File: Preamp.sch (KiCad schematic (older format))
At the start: 138 parts, among them J1 Conn_01x03, J10 RCAJack, J11 XLR4BODYPIN, J12 XLR4BODYPIN, J13 XLR4BODYPIN, J2 Conn_01x02, J3 Conn_01x02, J4 RCAJack, J5 RCAJack, J6 Conn_01x01, J7 Conn_01x01, J8 Conn_01x01, J9 Conn_01x01, SW1 SW_SPST, U1 LM317, U2 LM337, U3 LM4562, U4 LM4562, U5 LM4562, U6 LM4562, U7 LM4562, U8 LM4562

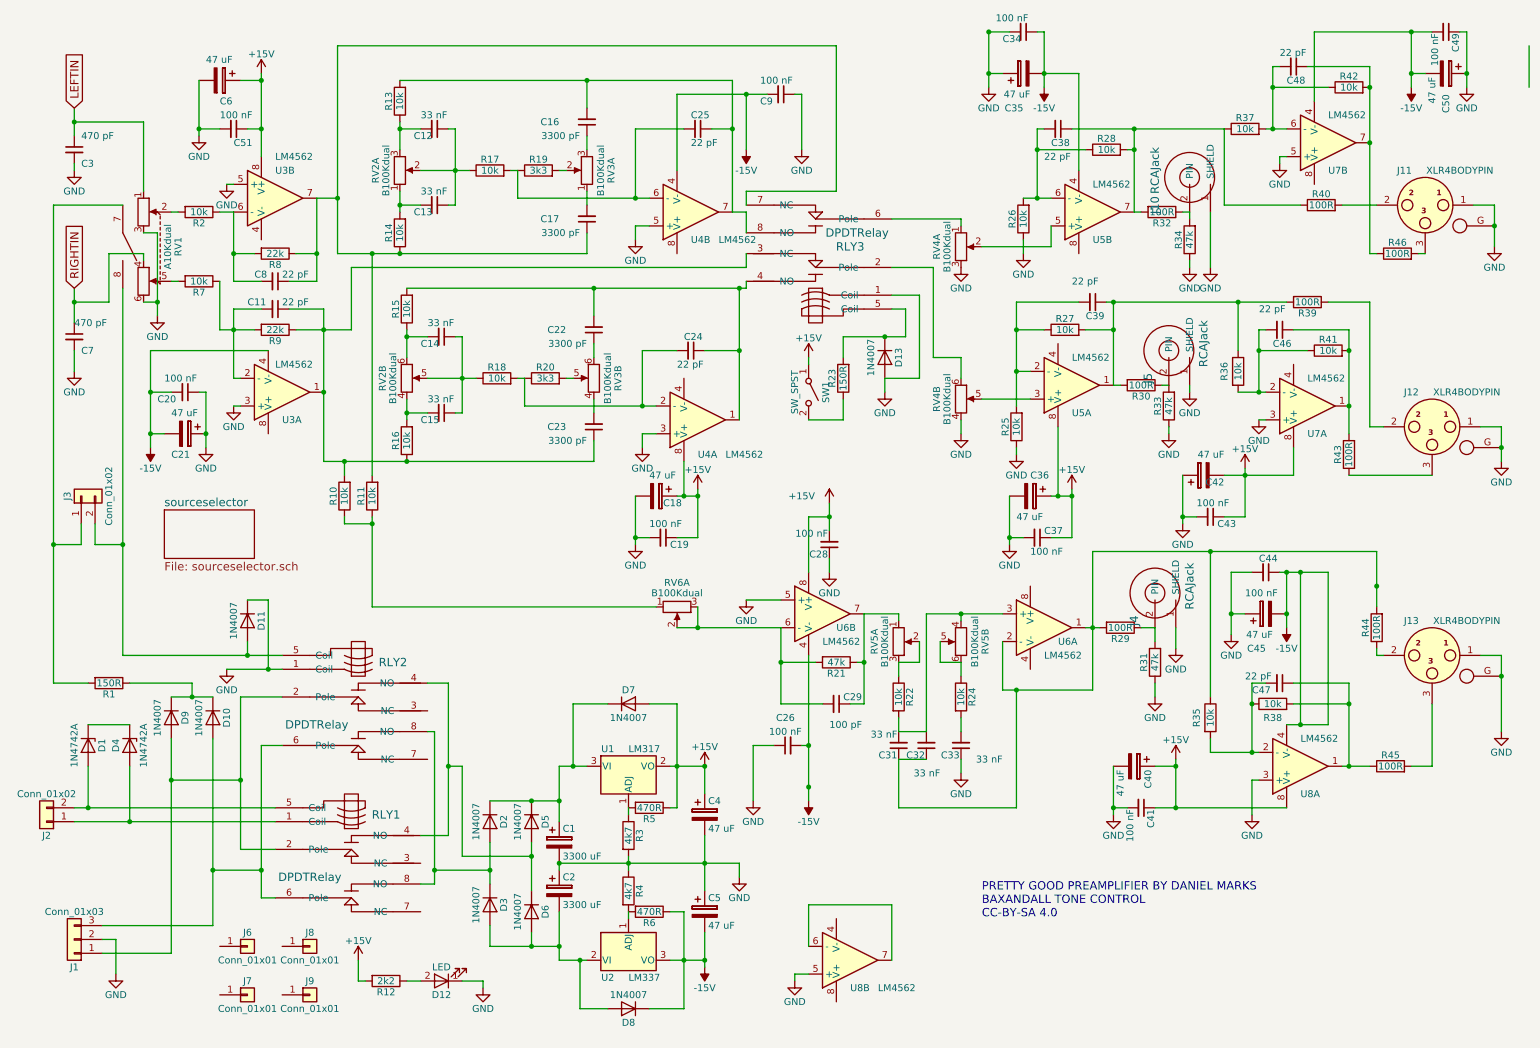
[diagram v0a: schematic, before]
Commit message: Changed balanced output to THAT1646
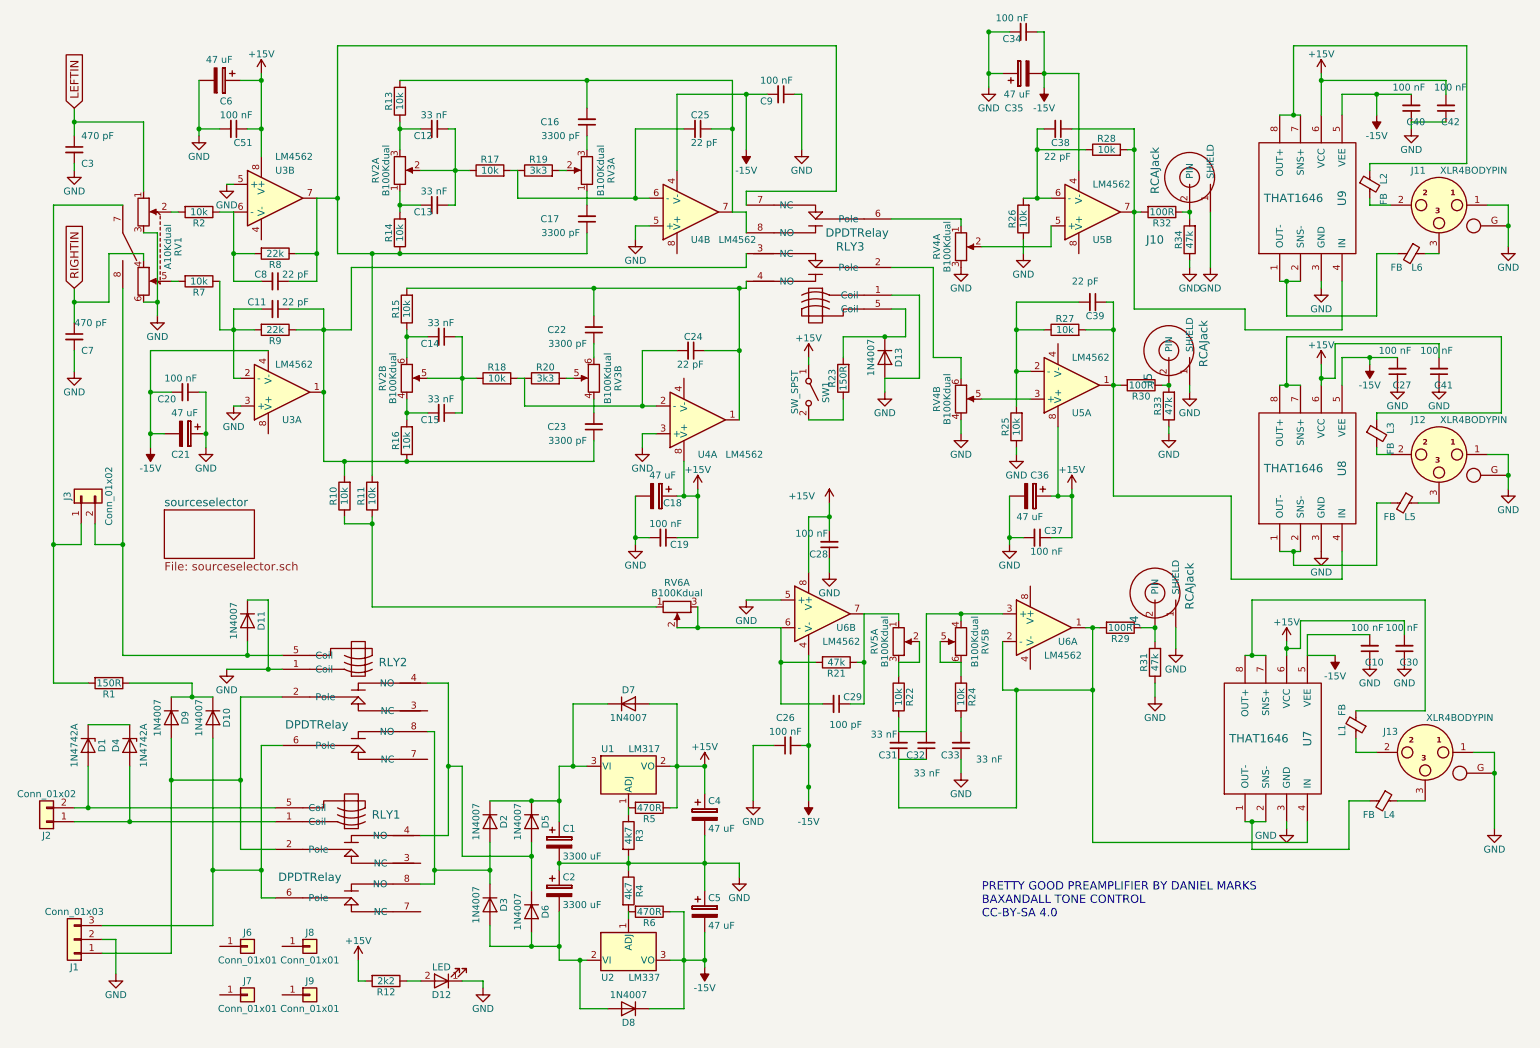
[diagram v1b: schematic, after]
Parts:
- removed C40, C42, C45, C50: 47 uF, Capacitors_THT:CP_Radial_D5.0mm_P2.50mm, symbol CP
- removed C43, C44, C49: 100 nF, Capacitors_THT:C_Disc_D5.0mm_W2.5mm_P5.00mm, symbol C_Small
- removed C46, C47, C48: 22 pF, Capacitors_THT:C_Disc_D5.0mm_W2.5mm_P5.00mm, symbol C_Small
- removed R35, R36, R37, R38, R41, R42: 10k, Resistors_THT:R_Axial_DIN0207_L6.3mm_D2.5mm_P7.62mm_Horizontal, symbol R
- removed R39, R40, R43, R44, R45, R46: 100R, Resistors_THT:R_Axial_DIN0207_L6.3mm_D2.5mm_P7.62mm_Horizontal, symbol R
- removed U7, U8: LM4562, Housings_DIP:DIP-8_W7.62mm, symbol TL072
- added C10, C27, C30, C40, C42: 100 nF, Capacitors_THT:C_Disc_D5.0mm_W2.5mm_P5.00mm, symbol C_Small
- added L1, L2, L3, L4, L5, L6: FB, Inductors_THT:L_Axial_L7.0mm_D3.3mm_P10.16mm_Horizontal_Fastron_MICC, symbol Ferrite_Bead_Small
- added U7, U8, U9: THAT1646, Housings_DIP:DIP-8_W7.62mm_Socket, symbol THAT1646
- U3, U4, U5, U6: footprint Housings_DIP:DIP-8_W7.62mm -> Housings_DIP:DIP-8_W7.62mm_Socket
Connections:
- net +15V: now also C41.2, C30.2, C42.2, U7.6 (VCC), U8.6 (VCC), U9.6 (VCC); no longer C41.1
- net -15V: now also C10.2, C27.2, C40.2, U7.5 (VEE), U8.5 (VEE), U9.5 (VEE)
- net GND: now also C41.1, C10.1, C27.1, C30.1, C40.1, C42.1, U7.3 (GND), U8.3 (GND), U9.3 (GND); no longer C41.2
- net at C31.1, C32.1, R29.2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: now also U7.4 (IN)
- net at J12.2: now also L3.2
- net at C39.1, R27.2, R30.2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: now also U8.4 (IN)
- net at J11.3: now also L6.1
- net at C38.1, R28.2, R32.2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: now also U9.4 (IN)
- net at J13.2: now also L1.1
- net at J12.3: now also L5.1
- net at J11.2: now also L2.2
- net at J13.3: now also L4.1
- new net: L6.2, U9.1 (OUT-), U9.2 (SNS-)
- new net: L2.1, U9.7 (SNS+), U9.8 (OUT+)
- new net: L5.2, U8.1 (OUT-), U8.2 (SNS-)
- new net: L3.1, U8.7 (SNS+), U8.8 (OUT+)
- new net: L4.2, U7.1 (OUT-), U7.2 (SNS-)
- new net: L1.2, U7.7 (SNS+), U7.8 (OUT+)
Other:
- moved on the sheet: J11, J12, J13

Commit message: Changed one input to be balanced
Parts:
- added C49, C52, C53: 47 uF, Capacitors_THT:CP_Radial_D5.0mm_P2.50mm, symbol CP
- added J25, J26, J27, J28: Conn_01x01, Connectors:1pin, symbol Conn_01x01
- added R34: 47k, Resistors_THT:R_Axial_DIN0207_L6.3mm_D2.5mm_P7.62mm_Horizontal, symbol R
- added R35, R36: 10k, Resistors_THT:R_Axial_DIN0207_L6.3mm_D2.5mm_P7.62mm_Horizontal, symbol R
- C50: renamed from R34; value 47k -> 47 uF; footprint Resistors_THT:R_Axial_DIN0207_L6.3mm_D2.5mm_P7.62mm_Horizontal -> Capacitors_THT:CP_Radial_D5.0mm_P2.50mm; symbol R -> CP
- R8, R9: value 22k -> 47k
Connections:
- net GND: now also R34.1; no longer C50.1
- net LEFTIN: now also C53.2; no longer C3.1, RV1.1
- net RIGHTIN: now also C52.2; no longer C7.1, RV1.4
- net at J10.2 (PIN), R32.1: now also R34.2; no longer C50.2
- new net: C50.2, C7.1, R36.1
- new net: C3.1, C49.2, R35.2
- new net: R35.1, RV1.1
- new net: R36.2, RV1.4
- new net: C49.1, C53.1
- new net: C50.1, C52.1
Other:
- moved on the sheet: C7, J6, J7, J8, J9

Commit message: JLCPCB 2021-03-26
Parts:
- RV1: footprint Preamp:Dual_Potentiometer_Switch_WirePads -> Preamp:Dual_Potentiometer_Switch_Wide_WirePads
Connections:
- no-connect marks 0 -> 12
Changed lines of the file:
@@
 F 0 "RV1" H 1400 2300 50  0000 C CNN
 F 1 "A10Kdual" H 1400 2225 50  0000 C CNN
-F 2 "Preamp:Dual_Potentiometer_Switch_WirePads" H 1650 2075 50  0001 C CNN
+F 2 "Preamp:Dual_Potentiometer_Switch_Wide_WirePads" H 1650 2075 50  0001 C CNN
 F 3 "" H 1650 2075 50  0001 C CNN
 	1    1400 2150
@@
 	4800 6950 4800 7000
 Wire Wire Line
-	4300 7300 4500 7300
-Wire Wire Line
 	4300 5900 4500 5900
 Wire Wire Line
@@
 Wire Wire Line
 	800  2450 800  2350
+Wire Wire Line
+	4300 7300 4500 7300
+NoConn ~ 2300 7100
+NoConn ~ 1850 7100
+NoConn ~ 1850 7400
+NoConn ~ 2300 7400
+NoConn ~ 2300 7700
+NoConn ~ 1850 7700
+NoConn ~ 1400 7700
+NoConn ~ 950  7700
+NoConn ~ 3300 6950
+NoConn ~ 3300 6600
+NoConn ~ 3350 5850
+NoConn ~ 3350 5500
 $EndSCHEMATC

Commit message: Pre off relay
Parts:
- removed R23: 150R, Resistors_THT:R_Axial_DIN0309_L9.0mm_D3.2mm_P12.70mm_Horizontal, symbol R
- added R37, R38, R39, R40: NC, Resistors_THT:R_Axial_DIN0207_L6.3mm_D2.5mm_P7.62mm_Horizontal, symbol R
- added R41, R42: 100R, Resistors_THT:R_Axial_DIN0411_L9.9mm_D3.6mm_P12.70mm_Horizontal, symbol R
- R10, R11: value 10k -> 47k
- R2, R7: value 10k -> 4k7
- R5, R6: value 470R -> 560R
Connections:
- net +15V: now also R41.1
- net -15V: now also C26.1, R42.2; no longer C26.2
- net GND: now also C26.2, D11.2 (A), R37.1, R38.2, R41.2, R42.1; no longer C26.1, D11.1 (K)
- net at R2.2, RV1.2: now also R37.2
- net at R7.2, RV1.5: now also R38.1
- net at J3.2 (Pin_2), RLY2.5 (Coil), RV1.8: now also D11.1 (K); no longer D11.2 (A)
- net at RLY3.6 (Pole), RV4.1 (4): now also R40.2
- net at RV4.2 (5), U5.5 (+): now also R40.1
- net at RV4.5, U5.3 (+): now also R39.1
- net at RLY3.2 (Pole), RV4.6: now also R39.2
- net at D13.1 (K), RLY3.5 (Coil): now also SW1.2 (B)
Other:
- moved on the sheet: C26

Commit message: Tried a relay version out
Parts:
- removed R41, R42: 100R, Resistors_THT:R_Axial_DIN0411_L9.9mm_D3.6mm_P12.70mm_Horizontal, symbol R
- C1, C2: value 3300 uF -> 47 uF; footprint Capacitors_THT:CP_Radial_D10.0mm_P5.00mm -> Capacitors_THT:CP_Radial_D7.5mm_P2.50mm
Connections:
- net at D9.2 (A), J1.1 (Pin_1), RLY1.2 (Pole): now also RLY2.6 (Pole); no longer RLY2.2 (Pole)
- net at D10.2 (A), J1.3 (Pin_3), RLY1.6 (Pole): now also RLY2.2 (Pole); no longer RLY2.6 (Pole)
- net at D2.2 (A), D3.1 (K), RLY1.8 (NO): now also RLY2.4 (NO); no longer RLY2.8 (NO)
- net at D5.2 (A), D6.1 (K), RLY1.4 (NO): now also RLY2.8 (NO); no longer RLY2.4 (NO)

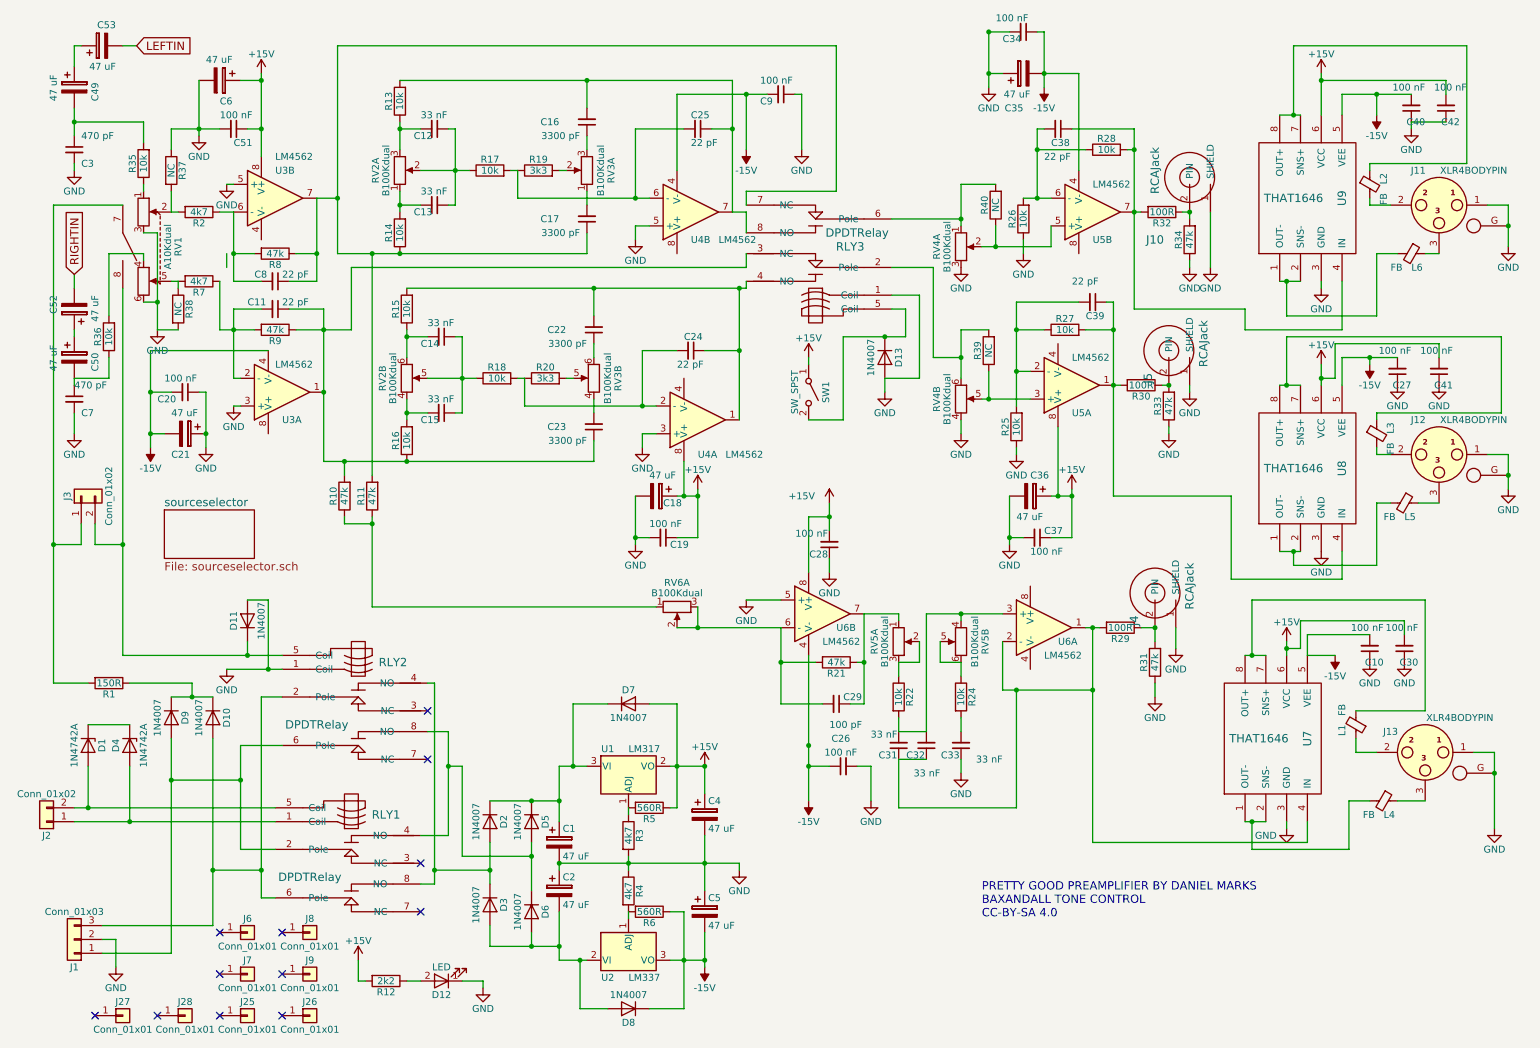
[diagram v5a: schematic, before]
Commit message: Put larger capacitors on
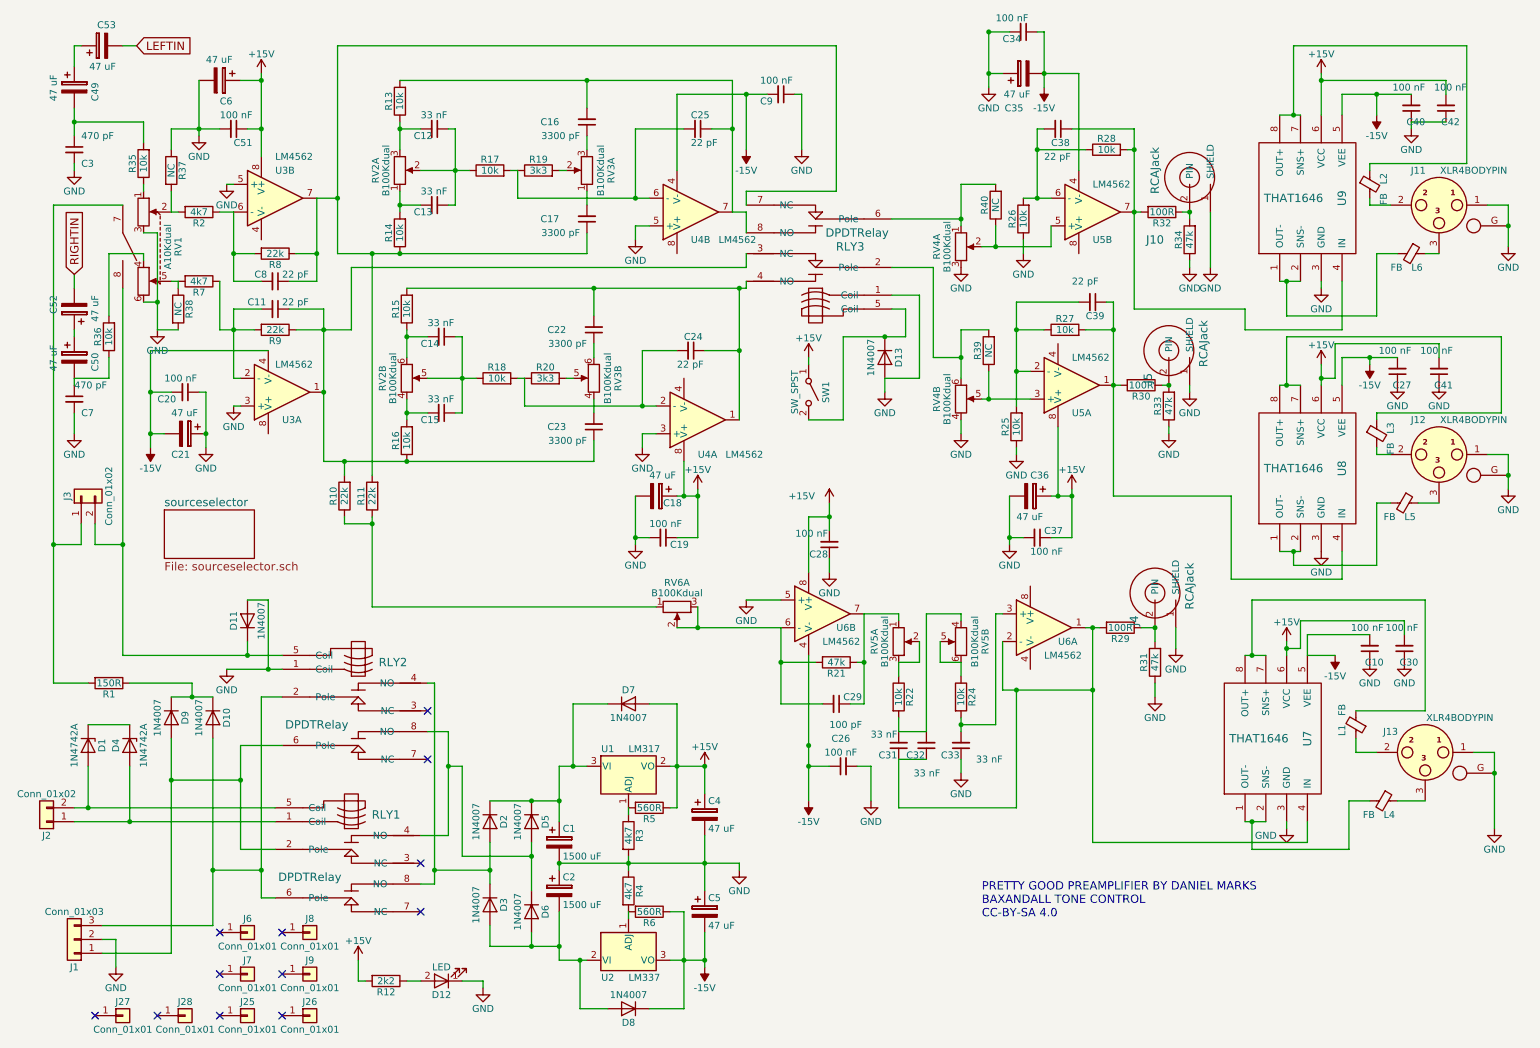
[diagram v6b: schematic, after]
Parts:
- C1, C2: value 47 uF -> 1500 uF; footprint Capacitors_THT:CP_Radial_D7.5mm_P2.50mm -> Capacitors_THT:CP_Radial_D10.0mm_P5.00mm
- R10, R11, R8, R9: value 47k -> 22k
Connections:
- net at C31.2, C32.2, R22.2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: no longer U6.3 (+)
- net at C33.2, R24.2: now also U6.3 (+)
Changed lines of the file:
@@
 P 4300 6450
 F 0 "C1" H 4325 6550 50  0000 L CNN
-F 1 "47 uF" H 4325 6350 50  0000 L CNN
-F 2 "Capacitors_THT:CP_Radial_D7.5mm_P2.50mm" H 4338 6300 50  0001 C CNN
+F 1 "1500 uF" H 4325 6350 50  0000 L CNN
+F 2 "Capacitors_THT:CP_Radial_D10.0mm_P5.00mm" H 4338 6300 50  0001 C CNN
 F 3 "" H 4300 6450 50  0001 C CNN
 	1    4300 6450
@@
 P 4300 6800
 F 0 "C2" H 4325 6900 50  0000 L CNN
-F 1 "47 uF" H 4325 6700 50  0000 L CNN
-F 2 "Capacitors_THT:CP_Radial_D7.5mm_P2.50mm" H 4338 6650 50  0001 C CNN
+F 1 "1500 uF" H 4325 6700 50  0000 L CNN
+F 2 "Capacitors_THT:CP_Radial_D10.0mm_P5.00mm" H 4338 6650 50  0001 C CNN
 F 3 "" H 4300 6800 50  0001 C CNN
 	1    4300 6800
@@
 P 2250 2200
 F 0 "R8" V 2330 2200 50  0000 C CNN
-F 1 "47k" V 2250 2200 50  0000 C CNN
+F 1 "22k" V 2250 2200 50  0000 C CNN
 F 2 "Resistors_THT:R_Axial_DIN0207_L6.3mm_D2.5mm_P7.62mm_Horizontal" V 2180 2200 50  0001 C CNN
 F 3 "" H 2250 2200 50  0001 C CNN
@@
 P 2250 2750
 F 0 "R9" V 2330 2750 50  0000 C CNN
-F 1 "47k" V 2250 2750 50  0000 C CNN
+F 1 "22k" V 2250 2750 50  0000 C CNN
 F 2 "Resistors_THT:R_Axial_DIN0207_L6.3mm_D2.5mm_P7.62mm_Horizontal" V 2180 2750 50  0001 C CNN
 F 3 "" H 2250 2750 50  0001 C CNN
@@
 P 2750 3950
 F 0 "R10" V 2830 3950 50  0000 C CNN
-F 1 "47k" V 2750 3950 50  0000 C CNN
+F 1 "22k" V 2750 3950 50  0000 C CNN
 F 2 "Resistors_THT:R_Axial_DIN0207_L6.3mm_D2.5mm_P7.62mm_Horizontal" V 2680 3950 50  0001 C CNN
 F 3 "" H 2750 3950 50  0001 C CNN
@@
 P 2950 3950
 F 0 "R11" V 3030 3950 50  0000 C CNN
-F 1 "47k" V 2950 3950 50  0000 C CNN
+F 1 "22k" V 2950 3950 50  0000 C CNN
 F 2 "Resistors_THT:R_Axial_DIN0207_L6.3mm_D2.5mm_P7.62mm_Horizontal" V 2880 3950 50  0001 C CNN
 F 3 "" H 2950 3950 50  0001 C CNN
@@
 Wire Wire Line
 	7500 5000 7500 5350
-Connection ~ 7200 4800
 Wire Wire Line
 	7200 5950 7200 5850
 Wire Wire Line
-	7200 5650 7200 5550
+	7200 5550 7200 5650
 Wire Wire Line
 	7200 5150 7200 5250
@@
 	7200 4800 7200 4850
 Wire Wire Line
-	6950 4800 7500 4800
+	6950 4800 7200 4800
 Wire Wire Line
-	6950 5650 6950 4800
+	7450 4800 7500 4800
 Wire Wire Line
 	6900 5150 6750 5150
@@
 Wire Wire Line
 	1500 1900 1500 1750
-Wire Wire Line
-	1900 2200 1900 2300
 $Comp
 L POT_Dual_SW RV1
@@
 	7200 1700 7450 1700
 Connection ~ 7200 1950
-$Comp
-L R R39
-U 1 1 605F2250
-P 7400 2900
-F 0 "R39" V 7480 2900 50  0000 C CNN
-F 1 "NC" V 7400 2900 50  0000 C CNN
-F 2 "Resistors_THT:R_Axial_DIN0207_L6.3mm_D2.5mm_P7.62mm_Horizontal" V 7330 2900 50  0001 C CNN
-F 3 "" H 7400 2900 50  0001 C CNN
-	1    7400 2900
-	-1   0    0    1
-$EndComp
 Wire Wire Line
 	7400 3050 7400 3250
@@
 Wire Wire Line
 	5600 6600 5600 6650
+Wire Wire Line
+	6950 4800 6950 5650
+$Comp
+L R R39
+U 1 1 606AABA8
+P 7400 2900
+F 0 "R39" V 7480 2900 50  0000 C CNN
+F 1 "NC" V 7400 2900 50  0000 C CNN
+F 2 "Resistors_THT:R_Axial_DIN0207_L6.3mm_D2.5mm_P7.62mm_Horizontal" V 7330 2900 50  0001 C CNN
+F 3 "" H 7400 2900 50  0001 C CNN
+	1    7400 2900
+	-1   0    0    1
+$EndComp
+Wire Wire Line
+	7200 5600 7450 5600
+Wire Wire Line
+	7450 5600 7450 4800
+Connection ~ 7200 5600
 $EndSCHEMATC
